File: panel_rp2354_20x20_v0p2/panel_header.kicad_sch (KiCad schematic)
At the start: 4 parts, among them J2 Conn_01x05, J3 Conn_01x05, J4 Conn_01x05, J5 Conn_01x05

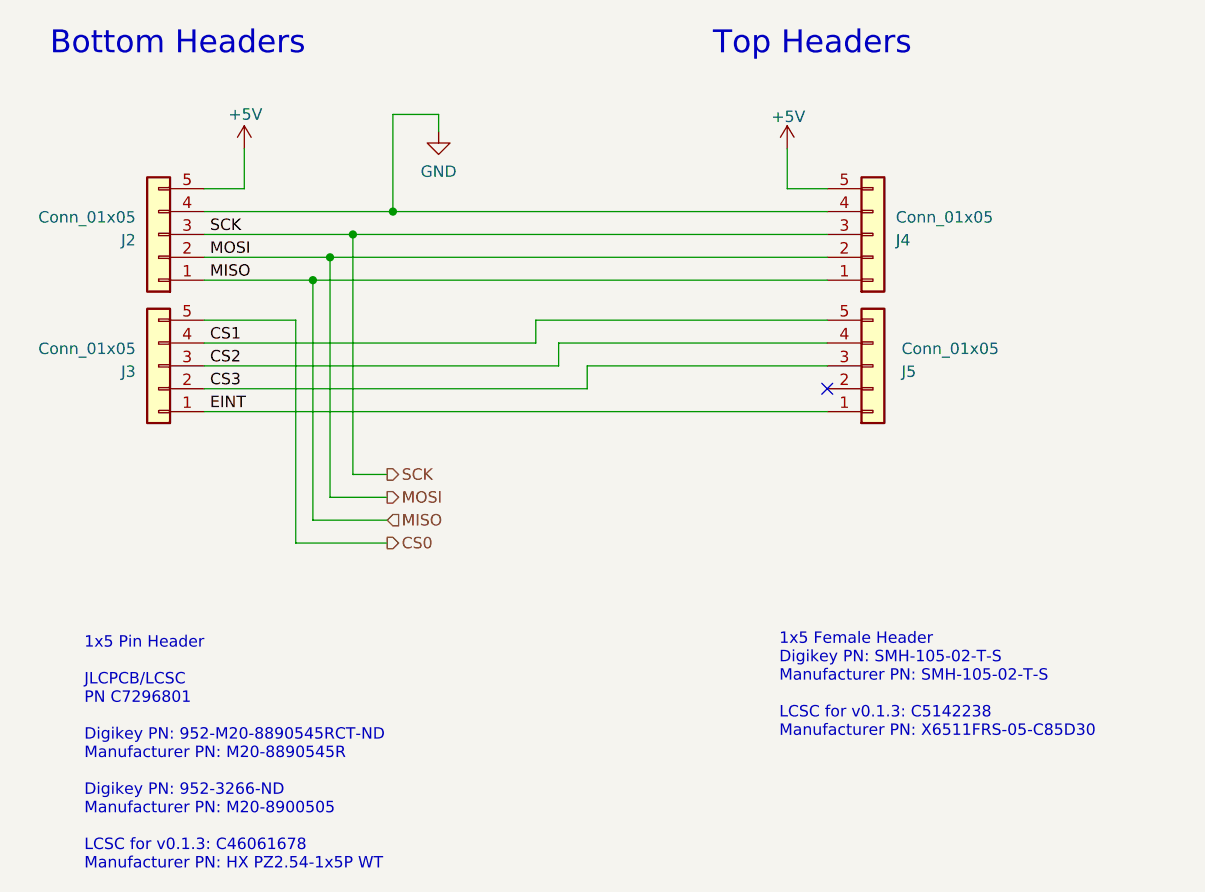
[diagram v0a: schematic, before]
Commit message: Route EINT and add MISO resistor
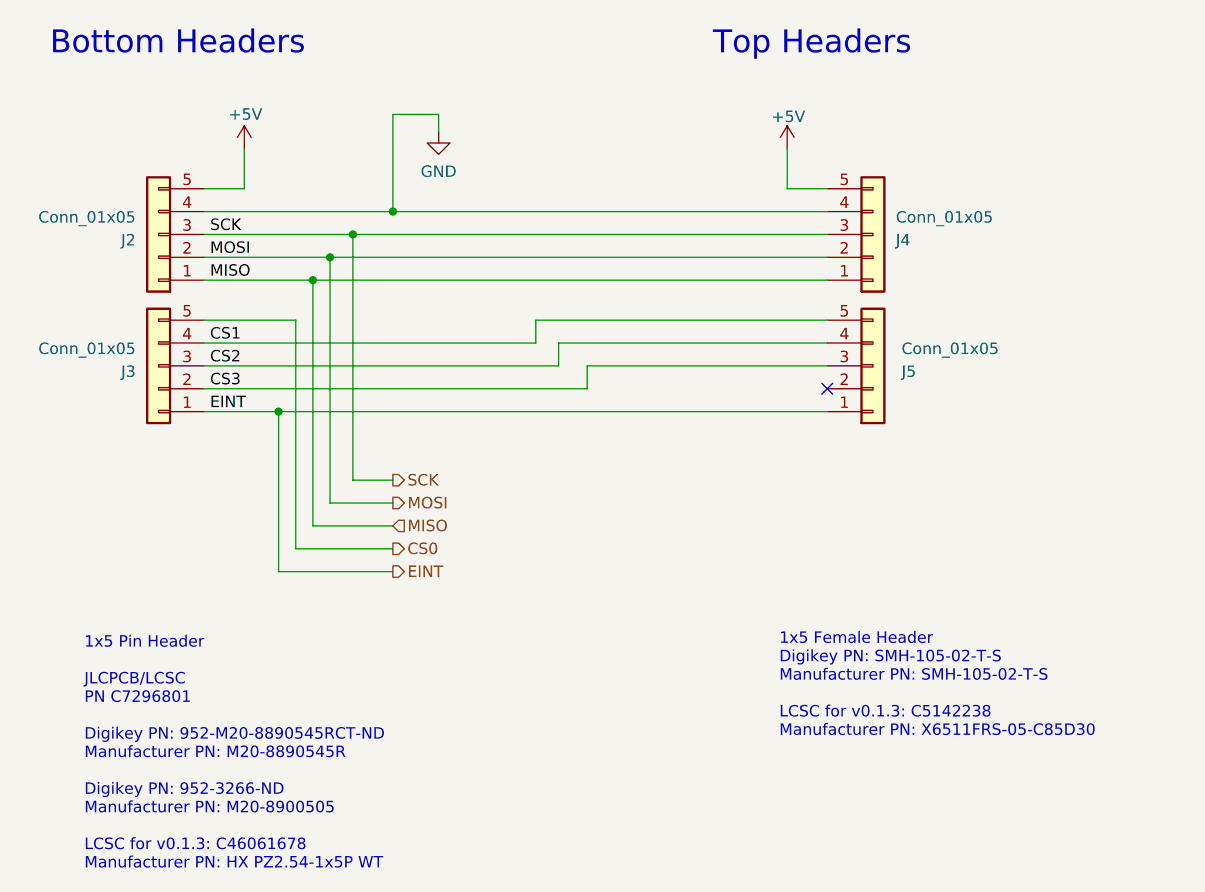
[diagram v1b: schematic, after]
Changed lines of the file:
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@@
+		(color 0 0 0 0)
+	)
+	(junction
+		(at 113.03 110.49)
+		(diameter 0)
 		(color 0 0 0 0)
 	)
@@
 	(wire
 		(pts
-			(xy 125.095 125.095) (xy 114.935 125.095)
-		)
-		(stroke
-			(width 0)
-			(type default)
-		)
-	)
-	(wire
-		(pts
-			(xy 104.775 110.49) (xy 173.99 110.49)
-		)
-		(stroke
-			(width 0)
-			(type default)
-		)
-	)
-	(wire
-		(pts
-			(xy 121.285 90.805) (xy 121.285 117.475)
+			(xy 125.73 125.73) (xy 114.935 125.73)
+		)
+		(stroke
+			(width 0)
+			(type default)
+		)
+	)
+	(wire
+		(pts
+			(xy 104.775 110.49) (xy 113.03 110.49)
+		)
+		(stroke
+			(width 0)
+			(type default)
+		)
+	)
+	(wire
+		(pts
+			(xy 121.285 90.805) (xy 121.285 118.11)
 		)
 		(stroke
@@
 	(wire
 		(pts
-			(xy 116.84 95.885) (xy 116.84 122.555)
+			(xy 116.84 95.885) (xy 116.84 123.19)
 		)
 		(stroke
@@
 	(wire
 		(pts
+			(xy 113.03 110.49) (xy 173.99 110.49)
+		)
+		(stroke
+			(width 0)
+			(type default)
+		)
+	)
+	(wire
+		(pts
 			(xy 144.145 102.87) (xy 173.99 102.87)
 		)
@@
 	(wire
 		(pts
-			(xy 118.745 120.015) (xy 125.095 120.015)
+			(xy 118.745 120.65) (xy 125.73 120.65)
 		)
 		(stroke
@@
 	(wire
 		(pts
-			(xy 116.84 122.555) (xy 125.095 122.555)
+			(xy 116.84 123.19) (xy 125.73 123.19)
 		)
 		(stroke
@@
 	(wire
 		(pts
-			(xy 114.935 125.095) (xy 114.935 100.33)
+			(xy 114.935 125.73) (xy 114.935 100.33)
 		)
 		(stroke
@@
 	(wire
 		(pts
+			(xy 113.03 128.27) (xy 125.73 128.27)
+		)
+		(stroke
+			(width 0)
+			(type default)
+		)
+	)
+	(wire
+		(pts
 			(xy 169.545 81.28) (xy 169.545 85.725)
 		)
@@
 	(wire
 		(pts
-			(xy 121.285 117.475) (xy 125.095 117.475)
+			(xy 121.285 118.11) (xy 125.73 118.11)
 		)
 		(stroke
@@
 	(wire
 		(pts
-			(xy 118.745 93.345) (xy 118.745 120.015)
+			(xy 113.03 128.27) (xy 113.03 110.49)
+		)
+		(stroke
+			(width 0)
+			(type default)
+		)
+	)
+	(wire
+		(pts
+			(xy 118.745 93.345) (xy 118.745 120.65)
 		)
 		(stroke
@@
 	(hierarchical_label "CS0"
 		(shape output)
-		(at 125.095 125.095 0)
+		(at 125.73 125.73 0)
 		(effects
 			(font
@@
 	(hierarchical_label "MOSI"
 		(shape output)
-		(at 125.095 120.015 0)
+		(at 125.73 120.65 0)
+		(effects
+			(font
+				(size 1.27 1.27)
+			)
+			(justify left)
+		)
+	)
+	(hierarchical_label "EINT"
+		(shape output)
+		(at 125.73 128.27 0)
 		(effects
 			(font
@@
 	(hierarchical_label "SCK"
 		(shape output)
-		(at 125.095 117.475 0)
+		(at 125.73 118.11 0)
 		(effects
 			(font
@@
 	(hierarchical_label "MISO"
 		(shape input)
-		(at 125.095 122.555 0)
-		(effects
-			(font
+		(at 125.73 123.19 0)
+		(effects
+			(font
